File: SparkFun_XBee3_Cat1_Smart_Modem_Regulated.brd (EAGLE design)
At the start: 35.6 x 52.1 mm, 97 parts, among them J4 QWIIC_RIGHT_ANGLE, U2 AP63203

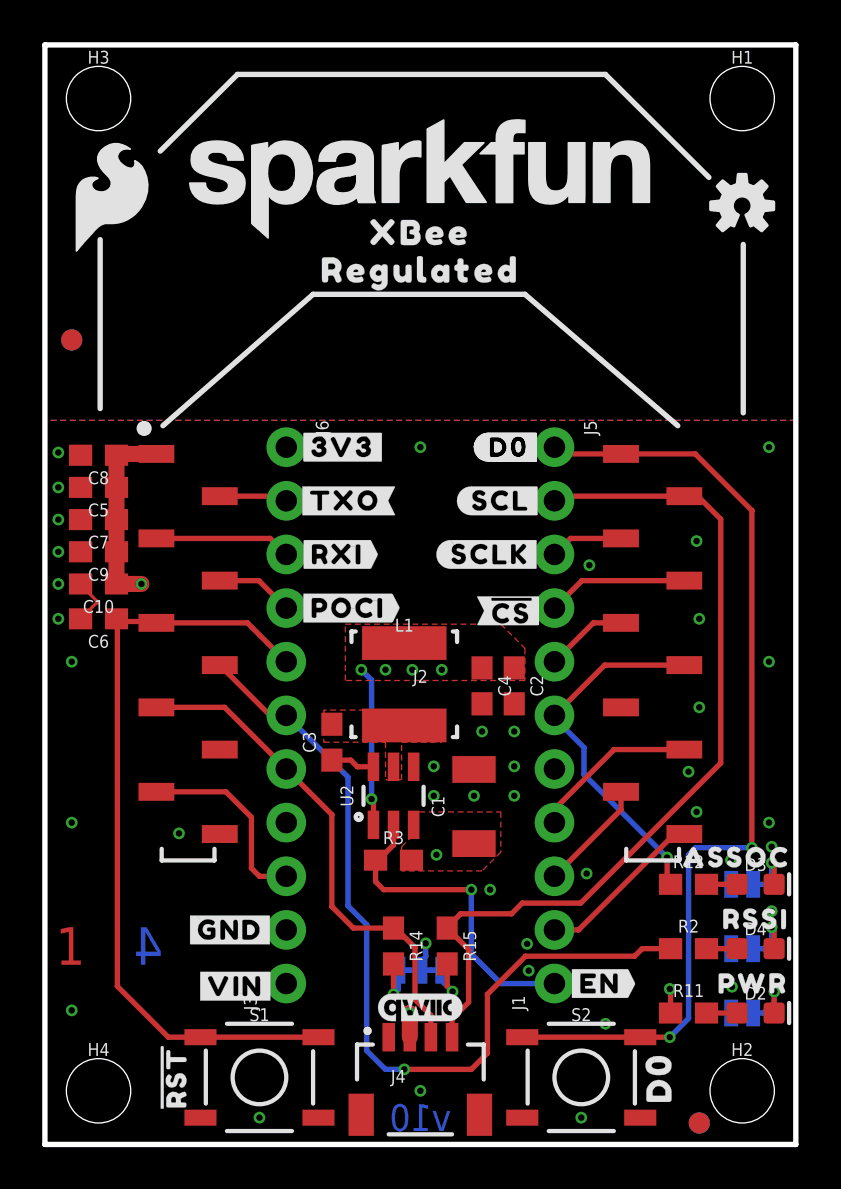
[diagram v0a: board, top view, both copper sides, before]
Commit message: Adds vias, fixes acid traps, moves LEDs away from the edge
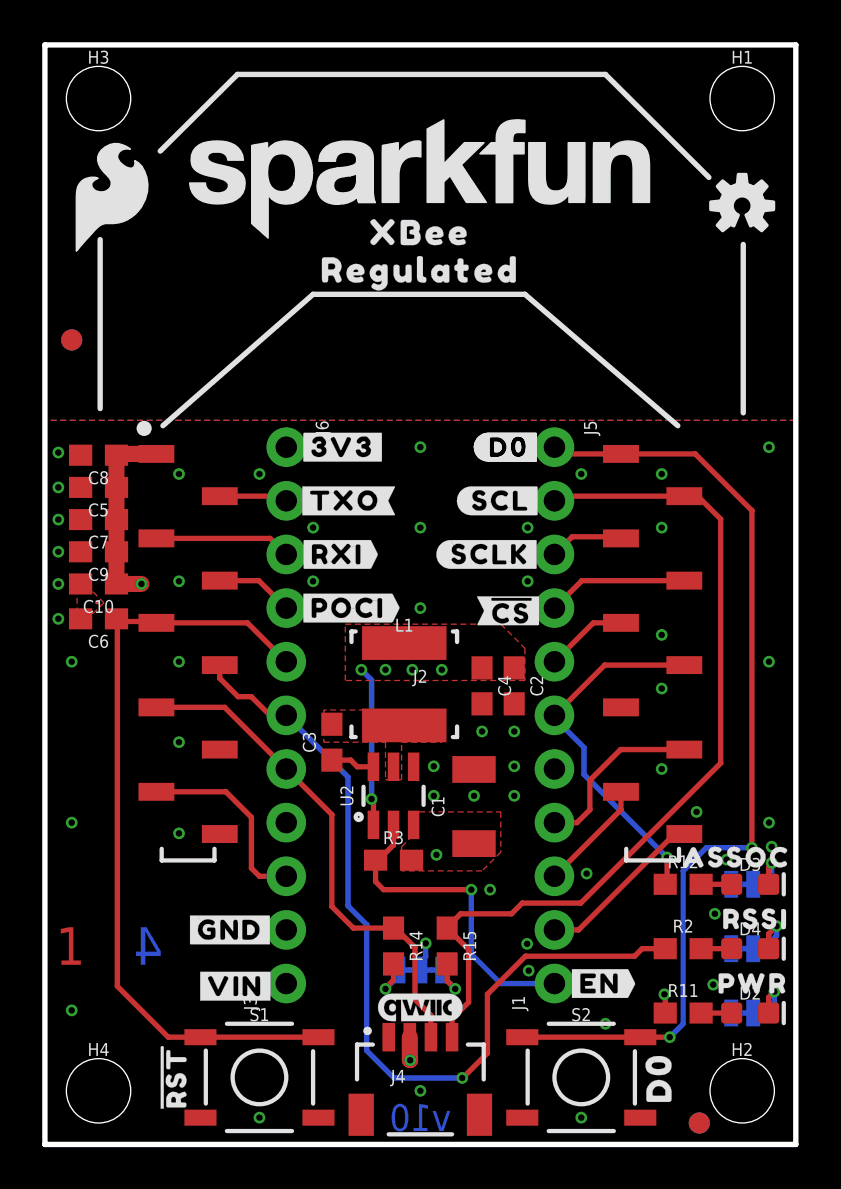
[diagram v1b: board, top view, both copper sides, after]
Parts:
- moved R11 0.25 mm to (29.0, 6.22)
- moved R12 0.25 mm to (29.0, 12.3)
- moved R2 0.25 mm to (29.0, 9.27)
- moved D2 0.25 mm to (32.1, 6.22)
- moved D3 0.25 mm to (32.1, 12.3)
- moved D4 0.25 mm to (32.1, 9.27)
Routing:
- net GND: track 2.41 -> 0.13 mm, vias 40 -> 52

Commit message: Moves I2C jumper down to make more space for the silk in that area
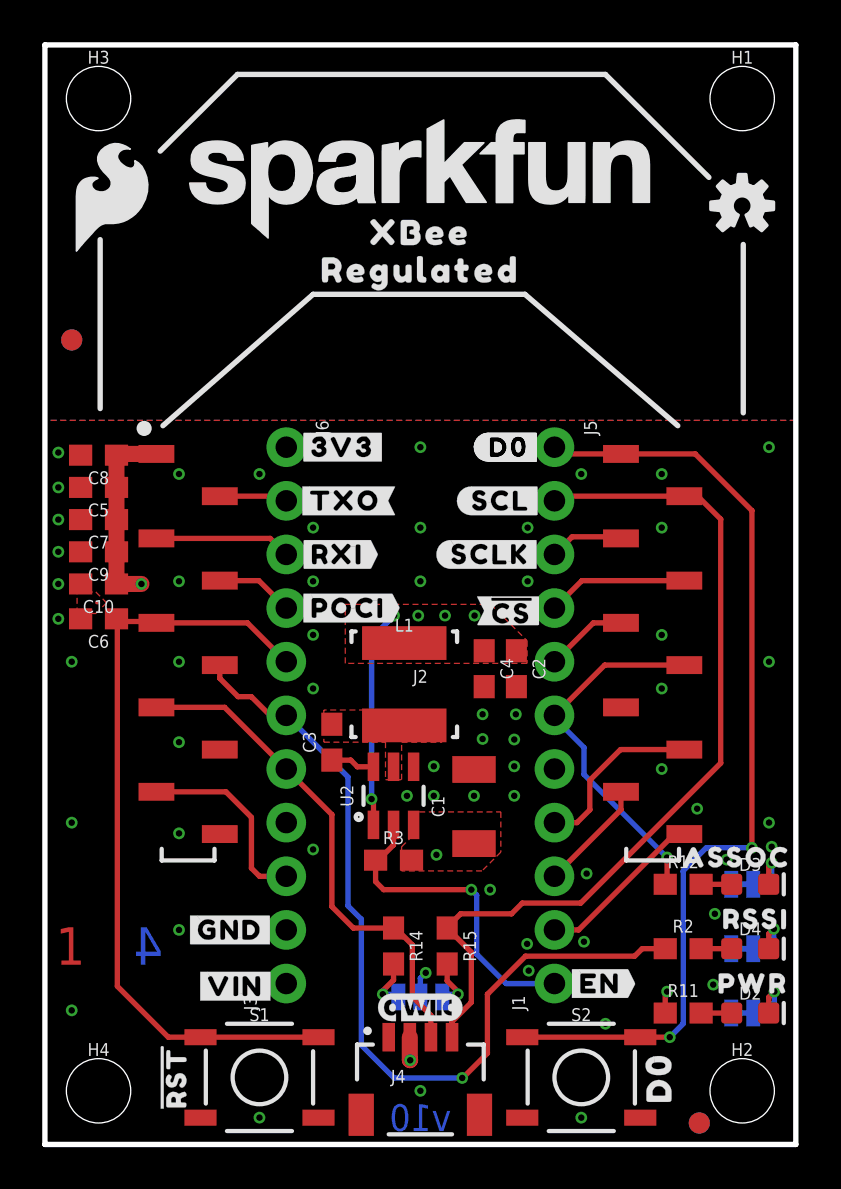
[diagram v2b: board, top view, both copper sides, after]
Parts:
- moved I2C_PU 1.27 mm to (16.5, 6.99)
- moved U$26 1.27 mm to (16.5, 5.21)
- moved C2 0.82 mm to (21.1, 22.5)
- moved C4 0.82 mm to (19.5, 22.5)
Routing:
- net 3.3V: track 20.2 -> 23.0 mm
- net GND: track 0.13 -> 0.09 mm, vias 52 -> 60

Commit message: Adds vias!!
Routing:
- net VIN: track 9.64 -> 10.2 mm, vias 1 -> 2
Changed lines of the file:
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@@
 <layers>
 <layer number="1" name="Top" color="4" fill="1" visible="yes" active="yes"/>
-<layer number="2" name="Route2" color="23" fill="1" visible="no" active="yes"/>
-<layer number="15" name="Route15" color="39" fill="1" visible="no" active="yes"/>
+<layer number="2" name="Route2" color="23" fill="1" visible="yes" active="yes"/>
+<layer number="15" name="Route15" color="39" fill="1" visible="yes" active="yes"/>
 <layer number="16" name="Bottom" color="3" fill="1" visible="yes" active="yes"/>
 <layer number="17" name="Pads" color="26" fill="1" visible="yes" active="yes"/>
@@
 </polygon>
 <contactref element="J3" pad="1"/>
-<wire x1="16.256" y1="13.716" x2="17.272" y2="13.716" width="0.762" layer="15"/>
-<via x="17.272" y="13.716" extent="1-16" drill="0.3048"/>
-<wire x1="10.16" y1="7.62" x2="16.256" y2="13.716" width="0.762" layer="15"/>
+<via x="17.018" y="14.097" extent="1-16" drill="0.3048"/>
+<wire x1="17.018" y1="14.097" x2="10.541" y2="7.62" width="0.762" layer="15"/>
+<wire x1="10.16" y1="7.62" x2="10.541" y2="7.62" width="0.762" layer="15"/>
+<via x="17.526" y="14.478" extent="1-16" drill="0.3048"/>
+<wire x1="17.526" y1="14.478" x2="17.145" y2="14.097" width="0.762" layer="15"/>
+<wire x1="17.018" y1="14.097" x2="17.145" y2="14.097" width="0.762" layer="15"/>
 </signal>
 <signal name="N$21">
